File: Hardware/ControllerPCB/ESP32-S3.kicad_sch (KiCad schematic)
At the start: 50 parts, among them J1 UJ20-C-H-G-SMT-1-P16-TR, J4 RJ45, J5 Conn_TagConnect_TC2030-NL_ESP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, U1 ESP32-S3-WROOM-1, U5 WE-TVS-82400102, U7 AP7333-33SRG-7

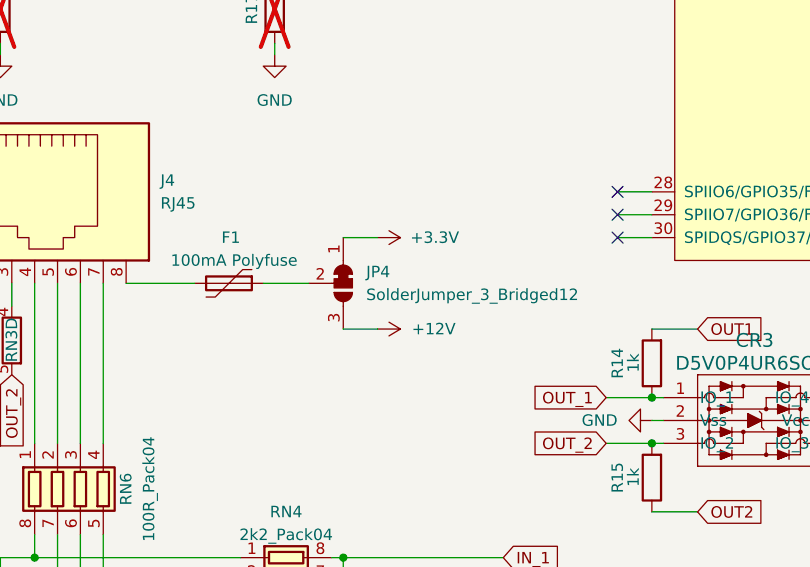
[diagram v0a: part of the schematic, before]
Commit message: update PCB and add a second PCB as a Controlpanel with a dual toggle switch and rgb LED
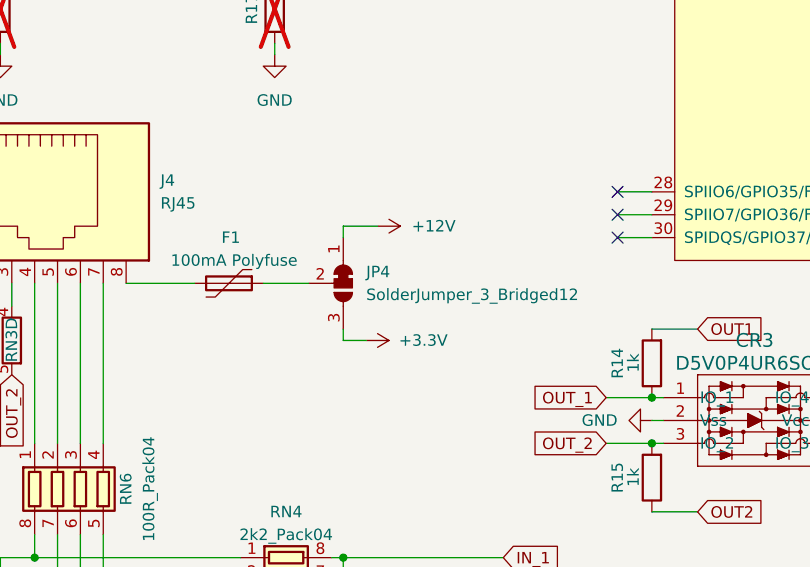
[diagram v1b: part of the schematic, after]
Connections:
- net +12V: now also JP4.1 (A); no longer JP4.3 (B)
- net +3.3V: now also JP4.3 (B); no longer JP4.1 (A)
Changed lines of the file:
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@@
     (stroke (width 0) (type default))
   )
+  (wire (pts (xy 67.31 144.78) (xy 67.31 143.51))
+    (stroke (width 0) (type default))
+  )
   (wire (pts (xy 214.63 22.86) (xy 214.63 20.32))
     (stroke (width 0) (type default))
@@
     (stroke (width 0) (type default))
   )
-  (wire (pts (xy 67.31 143.51) (xy 71.12 143.51))
-    (stroke (width 0) (type default))
-  )
   (wire (pts (xy 274.32 95.25) (xy 269.24 95.25))
     (stroke (width 0) (type default))
@@
     (stroke (width 0) (type default))
   )
-  (wire (pts (xy 67.31 133.35) (xy 71.12 133.35))
-    (stroke (width 0) (type default))
-  )
   (wire (pts (xy 156.21 33.02) (xy 156.21 31.75))
     (stroke (width 0) (type default))
@@
     (stroke (width 0) (type default))
   )
+  (wire (pts (xy 69.85 144.78) (xy 67.31 144.78))
+    (stroke (width 0) (type default))
+  )
   (wire (pts (xy 143.51 48.26) (xy 147.32 48.26))
     (stroke (width 0) (type default))
@@
     (stroke (width 0) (type default))
   )
+  (wire (pts (xy 67.31 133.35) (xy 67.31 132.08))
+    (stroke (width 0) (type default))
+  )
   (wire (pts (xy 193.04 125.73) (xy 196.85 125.73))
     (stroke (width 0) (type default))
@@
     (stroke (width 0) (type default))
   )
+  (wire (pts (xy 67.31 132.08) (xy 71.12 132.08))
+    (stroke (width 0) (type default))
+  )
   (wire (pts (xy 152.4 44.45) (xy 147.32 44.45))
     (stroke (width 0) (type default))
@@
     )
   )
-  (symbol (lib_id "power:+12V") (at 71.12 143.51 270) (unit 1)
+  (symbol (lib_id "power:+12V") (at 71.12 132.08 270) (unit 1)
     (in_bom yes) (on_board yes) (dnp no) (fields_autoplaced)
-    (property "Reference" "#PWR078" (at 67.31 143.51 0)
+    (property "Reference" "#PWR078" (at 67.31 132.08 0)
       (effects (font (size 1.27 1.27)) hide)
     )
-    (property "Value" "+12V" (at 74.93 143.51 90)
+    (property "Value" "+12V" (at 74.93 132.08 90)
       (effects (font (size 1.27 1.27)) (justify left))
     )
-    (property "Footprint" "" (at 71.12 143.51 0)
+    (property "Footprint" "" (at 71.12 132.08 0)
       (effects (font (size 1.27 1.27)) hide)
     )
-    (property "Datasheet" "" (at 71.12 143.51 0)
+    (property "Datasheet" "" (at 71.12 132.08 0)
       (effects (font (size 1.27 1.27)) hide)
     )
@@
     )
   )
-  (symbol (lib_id "power:+3.3V") (at 71.12 133.35 270) (unit 1)
+  (symbol (lib_id "power:+3.3V") (at 69.85 144.78 270) (unit 1)
     (in_bom yes) (on_board yes) (dnp no)
-    (property "Reference" "#PWR044" (at 67.31 133.35 0)
+    (property "Reference" "#PWR044" (at 66.04 144.78 0)
       (effects (font (size 1.27 1.27)) hide)
     )
-    (property "Value" "+3.3V" (at 77.47 133.35 90)
+    (property "Value" "+3.3V" (at 76.2 144.78 90)
       (effects (font (size 1.27 1.27)))
     )
-    (property "Footprint" "" (at 71.12 133.35 0)
+    (property "Footprint" "" (at 69.85 144.78 0)
       (effects (font (size 1.27 1.27)) hide)
     )
-    (property "Datasheet" "" (at 71.12 133.35 0)
+    (property "Datasheet" "" (at 69.85 144.78 0)
       (effects (font (size 1.27 1.27)) hide)
     )

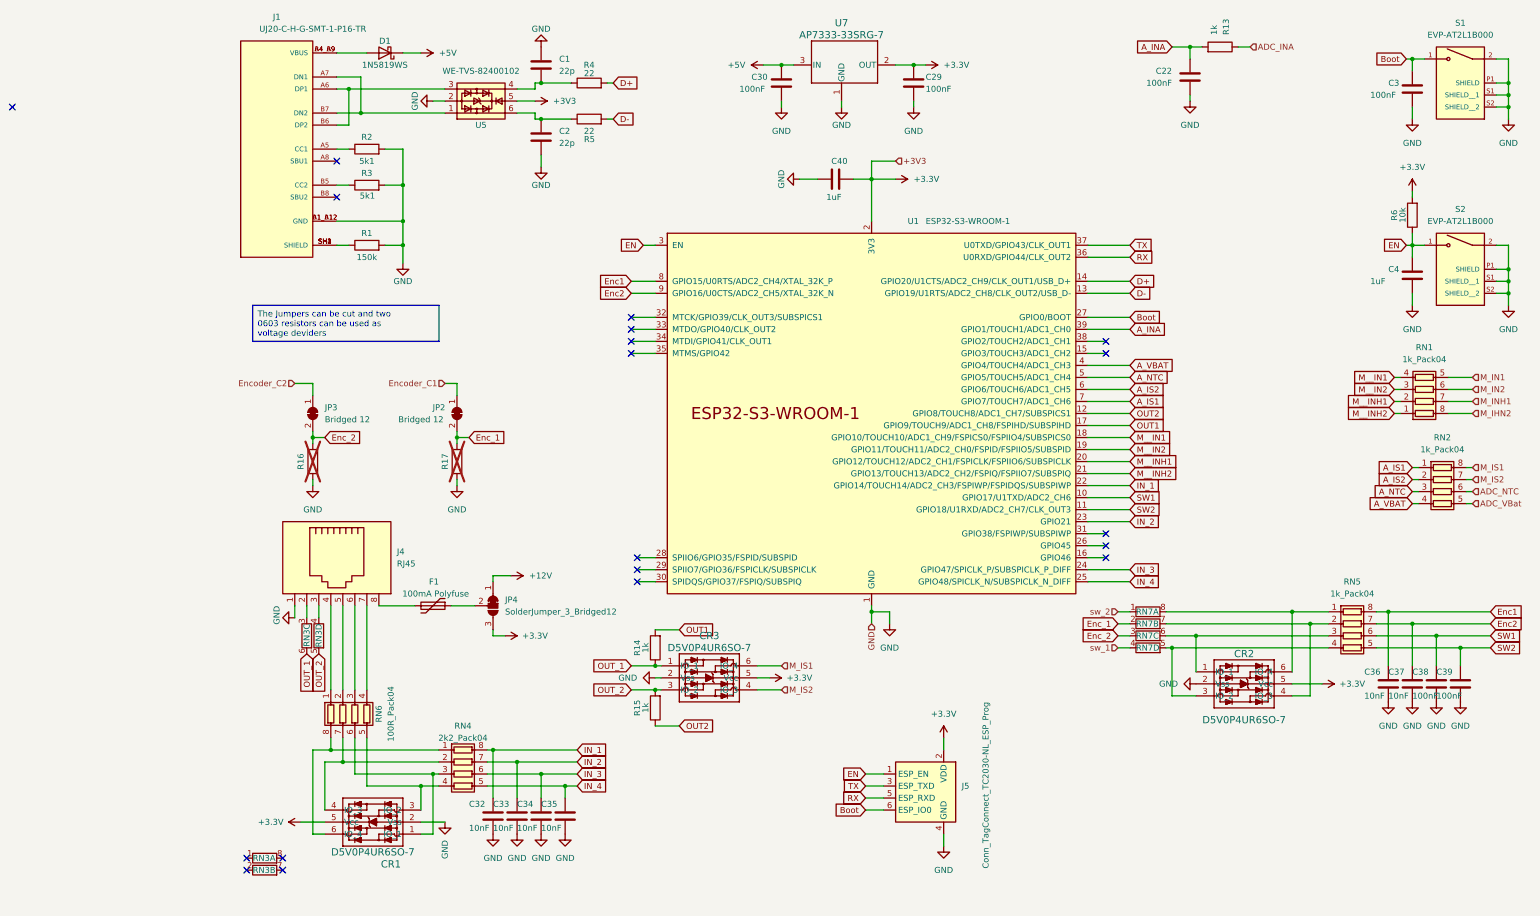
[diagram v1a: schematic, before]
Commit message: Add a micro SD Card slot to the bottom of the controller board
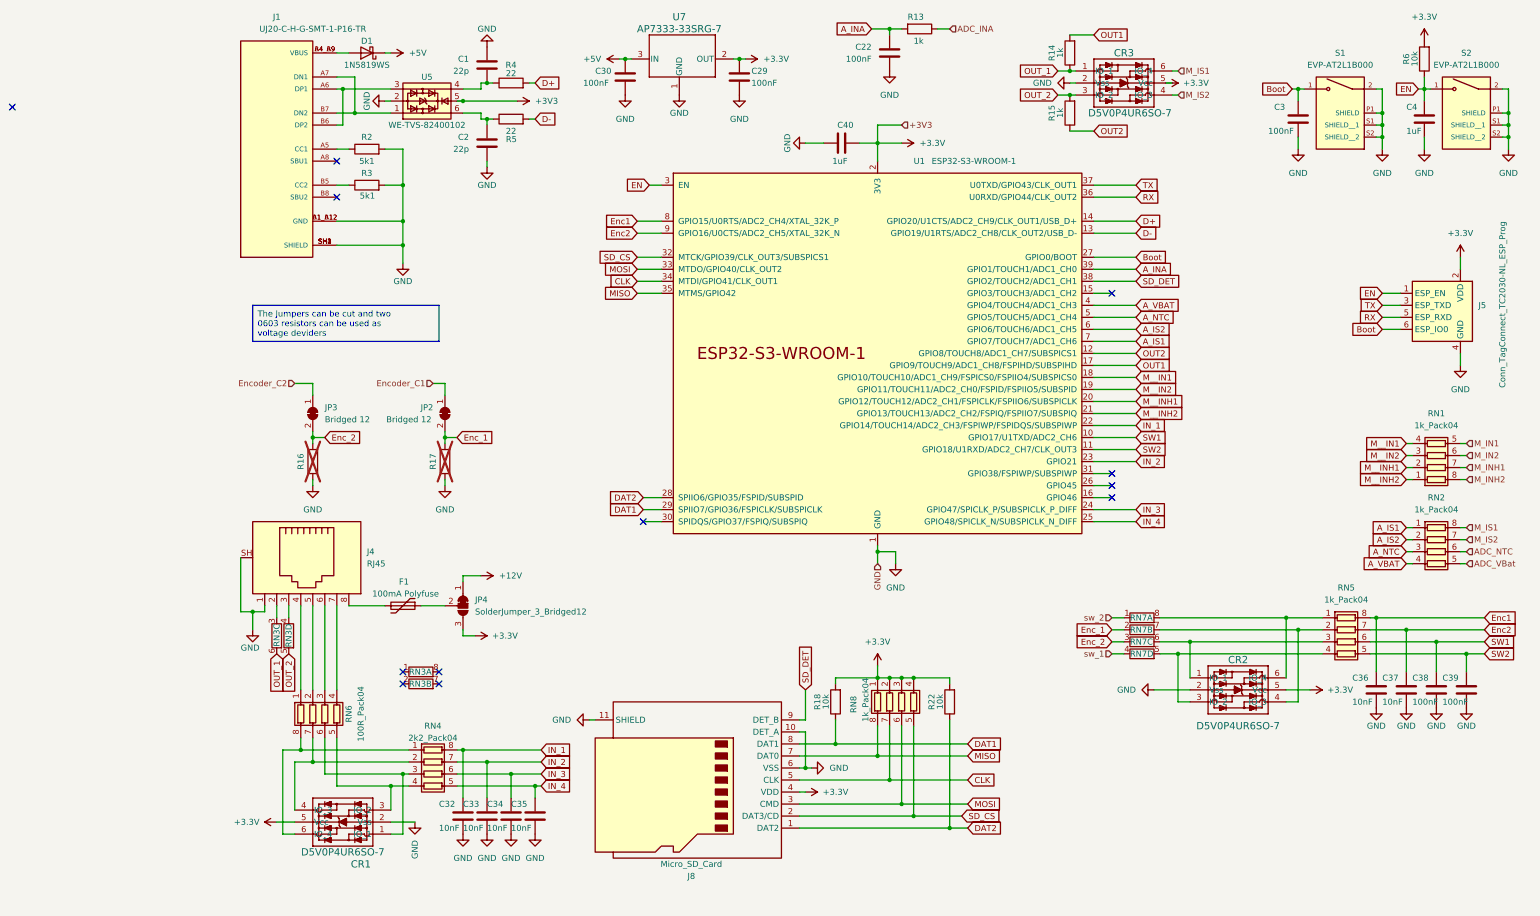
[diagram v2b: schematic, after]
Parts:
- removed R1: 150k, Resistor_SMD:R_0603_1608Metric, symbol Device:R
- added J8: Micro_SD_Card, BugWiper_lib:microSD_HC_Molex_104031-0811, symbol Connector:Micro_SD_Card_Det2
- added R18, R22: 10k, Resistor_SMD:R_0603_1608Metric, symbol Device:R
- added RN8: 1k_Pack04, BugWiper_lib:BO_CAY16, symbol Device:R_Pack04
- J4: symbol Connector:RJ45 -> Connector:RJ45_Shielded
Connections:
- net +3.3V: now also J8.4 (VDD), R18.2, R22.2, RN8.1 (R1.1), RN8.2 (R2.1), RN8.3 (R3.1), RN8.4 (R4.1)
- net GND: now also J1.SH1 (SHIELD), J1.SH2 (SHIELD), J1.SH3 (SHIELD), J1.SH4 (SHIELD), J4.SH, J8.10 (DET_A), J8.11 (SHIELD), J8.6 (VSS)
- net DAT2: now reaches U1.28 (SPIIO6/GPIO35/FSPID/SUBSPID)
- net DAT2: now also J8.1 (DAT2), R22.1
- net DAT1: now reaches U1.29 (SPIIO7/GPIO36/FSPICLK/SUBSPICLK)
- net DAT1: now also J8.8 (DAT1), R18.1
- net SD_CS: now reaches U1.32 (MTCK/GPIO39/CLK_OUT3/SUBSPICS1)
- net SD_CS: now also J8.2 (DAT3/CD), RN8.5 (R4.2)
- net MOSI: now reaches U1.33 (MTDO/GPIO40/CLK_OUT2)
- net MOSI: now also J8.3 (CMD), RN8.6 (R3.2)
- net CLK: now reaches U1.34 (MTDI/GPIO41/CLK_OUT1)
- net CLK: now also J8.5 (CLK), RN8.7 (R2.2)
- net MISO: now reaches U1.35 (MTMS/GPIO42)
- net MISO: now also J8.7 (DAT0), RN8.8 (R1.2)
- net SD_DET: now reaches U1.38 (GPIO2/TOUCH2/ADC1_CH1)
- net SD_DET: now also J8.9 (DET_B)
- net M_IHN2 renamed M_INH2
- no-connect marks 19 -> 12
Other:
- moved on the sheet: C1, C2, C22, C29, C3, C30, C32, C33, C34, C35, C36, C37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

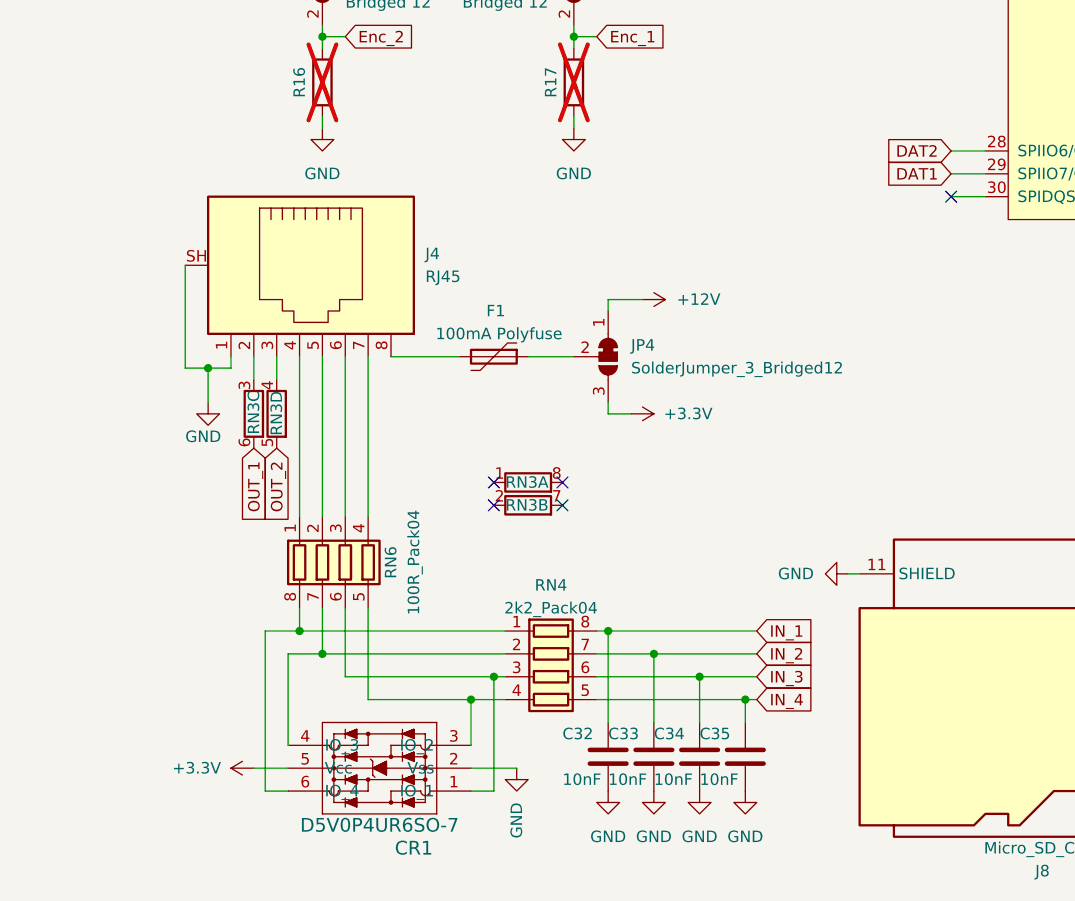
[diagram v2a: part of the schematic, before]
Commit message: update Controller PCB
Add Fuses for GND Signal Connectors, fix 3D and fix DRC
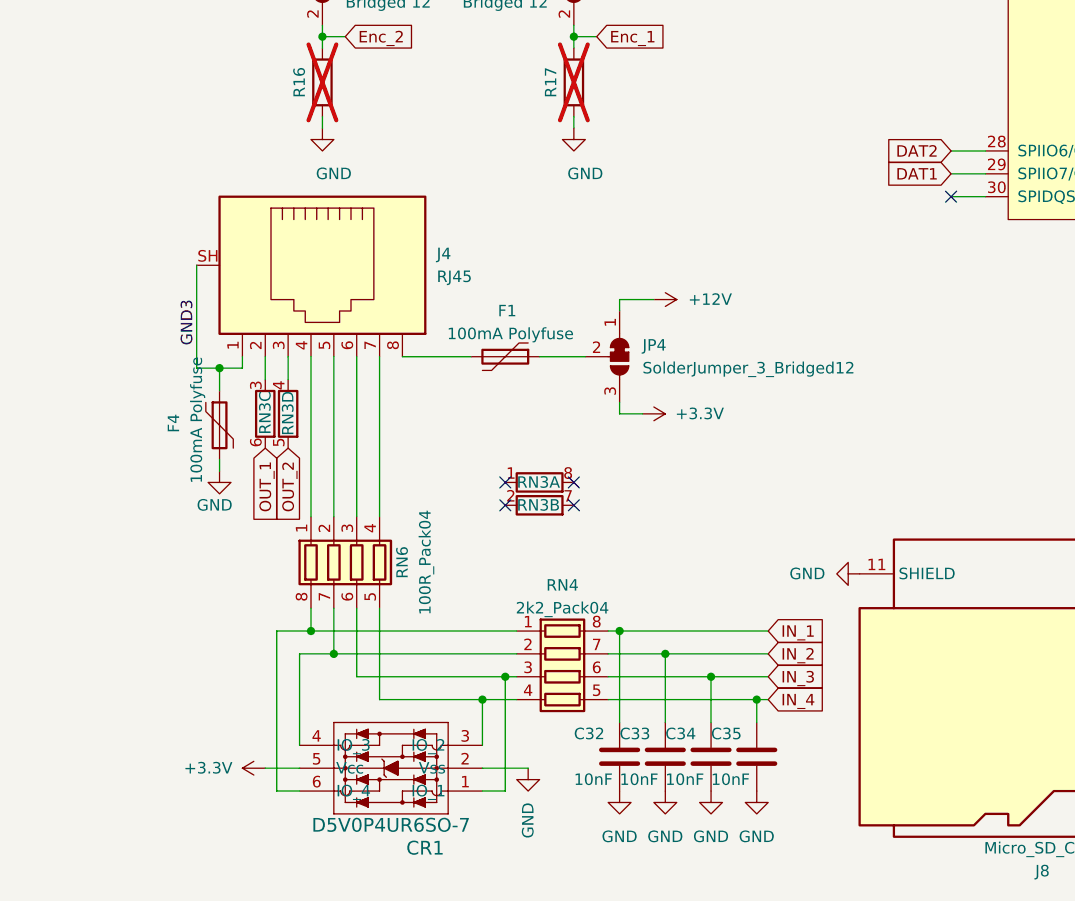
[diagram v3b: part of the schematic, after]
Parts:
- added F4: 100mA Polyfuse, Resistor_SMD:R_1206_3216Metric, symbol Device:Polyfuse
- F1: MP (none) -> PTS120630V012; Manufacturer_Name (none) -> Eaton Electronics; Manufacturer_Part_Number (none) -> PTS120630V012; Price (none) -> 0,108€
- J1: Manufacturer_Name (none) -> Same Sky; Manufacturer_Part_Number (none) -> UJ20-C-H-G-SMT-1-P16-TR
- S1, S2: Manufacturer_Name (none) -> Panasonic
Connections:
- net GND: now also F4.2; no longer J4.1, J4.SH
- new net GND3: F4.1, J4.1, J4.SH
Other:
- moved on the sheet: C32, C33, C34, C35, CR1, F1, J4, JP4, RN3A, RN3B, RN3C, RN3D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

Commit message: Update PCB
Add solder jumper for +3.3V selection
fix DRC
aligne vias
export Gerber
add text
fix 3D Models
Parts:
- added JP5: SolderJumper_2_Open, Jumper:SolderJumper-2_P1.3mm_Open_TrianglePad1.0x1.5mm, symbol Jumper:SolderJumper_2_Open
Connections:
- net +3.3V: now also JP5.2 (B); no longer C29.1, U7.2 (OUT)
- new net +3,3V: C29.1, JP5.1 (A), U7.2 (OUT)
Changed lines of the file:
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@@
     (effects (font (size 1.27 1.27)) (justify left top))
+  )
+  (label "+3,3V" (at 118.11 22.86 0) (fields_autoplaced)
+    (effects (font (size 1.27 1.27)) (justify left bottom))
   )
   (label "GND3" (at 15.24 137.16 90) (fields_autoplaced)
@@
     )
   )
-  (symbol (lib_id "power:+3.3V") (at 120.65 22.86 270) (unit 1)
+  (symbol (lib_id "power:+3.3V") (at 128.27 22.86 270) (unit 1)
     (in_bom yes) (on_board yes) (dnp no) (fields_autoplaced)
-    (property "Reference" "#PWR014" (at 116.84 22.86 0)
-      (effects (font (size 1.27 1.27)) hide)
-    )
-    (property "Value" "+3.3V" (at 124.46 22.86 90)
-      (effects (font (size 1.27 1.27)) (justify left))
-    )
-    (property "Footprint" "" (at 120.65 22.86 0)
-      (effects (font (size 1.27 1.27)) hide)
-    )
-    (property "Datasheet" "" (at 120.65 22.86 0)
+    (property "Reference" "#PWR014" (at 124.46 22.86 0)
+      (effects (font (size 1.27 1.27)) hide)
+    )
+    (property "Value" "+3.3V" (at 132.08 22.86 90)
+      (effects (font (size 1.27 1.27)) (justify left))
+    )
+    (property "Footprint" "" (at 128.27 22.86 0)
+      (effects (font (size 1.27 1.27)) hide)
+    )
+    (property "Datasheet" "" (at 128.27 22.86 0)
       (effects (font (size 1.27 1.27)) hide)
     )
@@
         )
       )
+    )
+  )
+  (symbol (lib_id "Jumper:SolderJumper_2_Open") (at 124.46 22.86 0) (unit 1)
+    (in_bom yes) (on_board yes) (dnp no)
+    (property "Reference" "JP5" (at 124.46 16.51 0)
+      (effects (font (size 1.27 1.27)))
+    )
+    (property "Value" "SolderJumper_2_Open" (at 127 19.05 0)
+      (effects (font (size 1.27 1.27)))
+    )
+    (property "Footprint" "Jumper:SolderJumper-2_P1.3mm_Open_TrianglePad1.0x1.5mm" (at 124.46 22.86 0)
+      (effects (font (size 1.27 1.27)) hide)
+    )
+    (property "Datasheet" "~" (at 124.46 22.86 0)
+      (effects (font (size 1.27 1.27)) hide)
+    )
+    (pin "1")
+    (pin "2")
+    (instances
+      (project "BugWiperPCB"
+        (path "/d31a15bd-db02-4d4c-9593-17c596d3182c/caaad550-b4dc-4462-8f3c-cac307d6a6e2"
+          (reference "JP5") (unit 1)
+        )
+      )
